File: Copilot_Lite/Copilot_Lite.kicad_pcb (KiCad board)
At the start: 4 copper layers, 65 x 56 mm, 80 parts, among them J1 POWER_MODES, J11 SERIAL_MODE, J12 SERIAL_VOLTAGE_SELECT, J2 JACK_POWER_IN, J3 USB_POWER_IN, J4 USB_PC, J6 5V_ENABLE, J7 SERIAL_AND_GPIO, J8 JACK_POWER_OUT, J9 USB_POWER_OUT, Q1 BSS138, Q2 BUK7M27-80EX, Q3 BUK7M27-80EX, Q4 BSS138, Q5 BSS138, Q6 BSS138, Q7 BSS138, Q8 BSS138, Q9 BSS138, U1 LM74502, U2 LM74502, U3 AP2204K-ADJ, U4 AP2204K-ADJ, U5 FT230XS, U6 SN74LV1T125, U7 SN74LV1T125, U8 SN74LV1T125, U9 SN74LV1T125

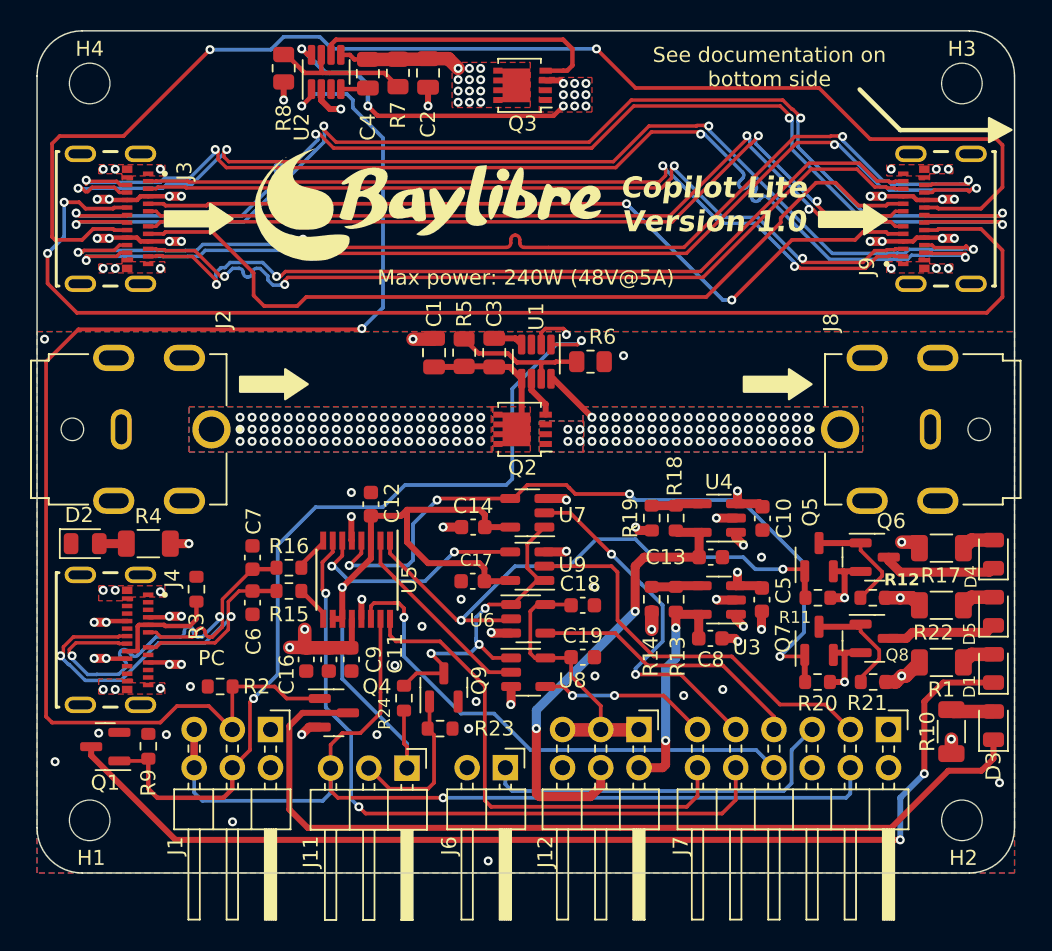
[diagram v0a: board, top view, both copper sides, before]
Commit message: lite: Added a little offset to the USB-C connector shield pins to make sure the connector is well aligned when being soldered.
Signed-off-by: Adrien Ricciardi <aricciardi@baylibre.com>
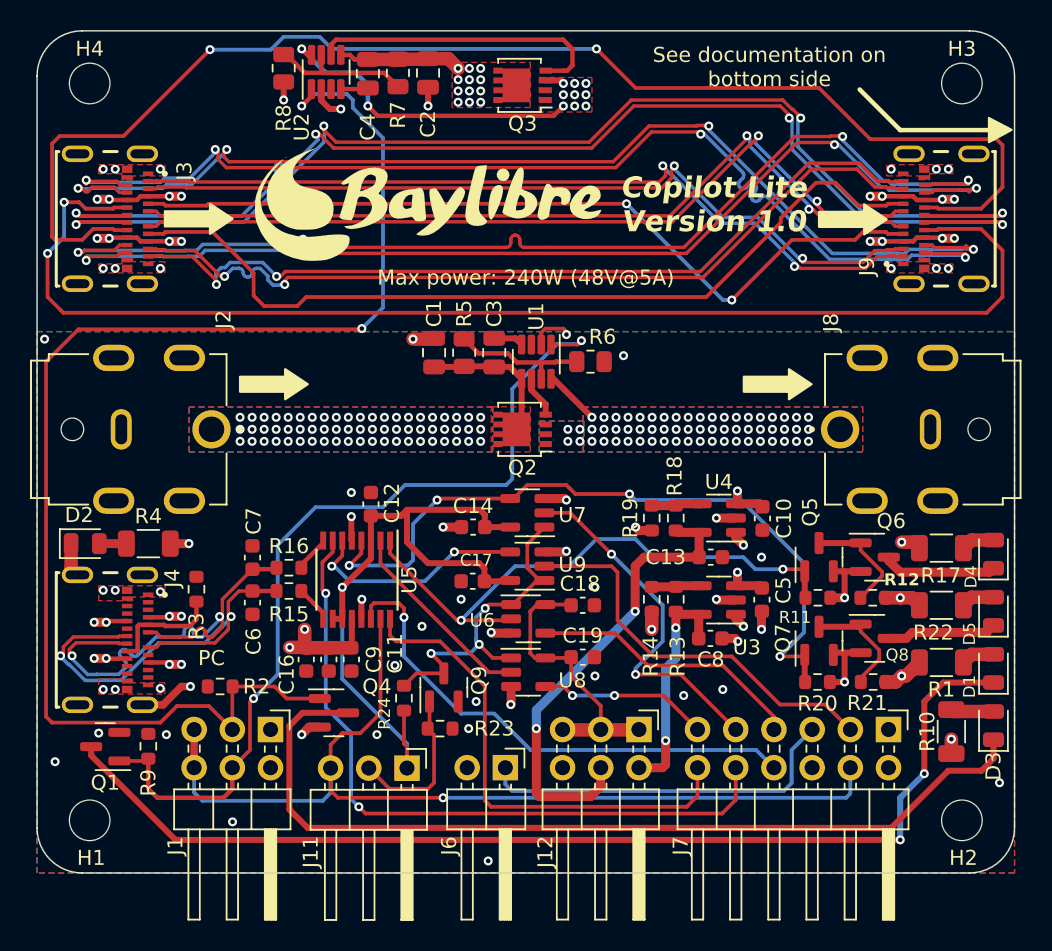
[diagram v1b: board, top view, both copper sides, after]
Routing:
- net GND: track 36.8 -> 42.8 mm
- net /SBU2: track 83.9 -> 84.4 mm
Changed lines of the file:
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@@
     (pad "B12" smd rect (at -2.75 -2.54 90) (size 0.3 0.7) (layers "F.Cu" "F.Paste" "F.Mask")
       (net 2 "GND") (pinfunction "GND_B") (pintype "passive"))
-    (pad "S1" thru_hole oval (at -4.32 0.57 90) (size 1.1 2.1) (drill oval 0.6 1.6) (layers "*.Cu" "*.Mask")
+    (pad "S1" thru_hole oval (at -4.322 0.762 90) (size 1.1 2.1) (drill oval 0.6 1.6) (layers "*.Cu" "*.Mask")
       (net 2 "GND") (pinfunction "SHIELD") (pintype "passive"))
-    (pad "S2" thru_hole oval (at 4.32 0.57 90) (size 1.1 2.1) (drill oval 0.6 1.6) (layers "*.Cu" "*.Mask")
+    (pad "S2" thru_hole oval (at 4.318 0.762 90) (size 1.1 2.1) (drill oval 0.6 1.6) (layers "*.Cu" "*.Mask")
       (net 2 "GND") (pinfunction "SHIELD") (pintype "passive"))
-    (pad "S3" thru_hole oval (at -4.32 -3.43 90) (size 1.1 2.1) (drill oval 0.6 1.6) (layers "*.Cu" "*.Mask")
+    (pad "S3" thru_hole oval (at -4.32 -3.556 90) (size 1.1 2.1) (drill oval 0.6 1.6) (layers "*.Cu" "*.Mask")
       (net 2 "GND") (pinfunction "SHIELD") (pintype "passive"))
-    (pad "S4" thru_hole oval (at 4.32 -3.43 90) (size 1.1 2.1) (drill oval 0.6 1.6) (layers "*.Cu" "*.Mask")
+    (pad "S4" thru_hole oval (at 4.32 -3.556 90) (size 1.1 2.1) (drill oval 0.6 1.6) (layers "*.Cu" "*.Mask")
       (net 2 "GND") (pinfunction "SHIELD") (pintype "passive"))
     (pad "S5" smd rect (at -3.3 -2.54 90) (size 0.5 0.7) (layers "F.Cu" "F.Paste" "F.Mask")
@@
         (effects (font (size 1 1) (thickness 0.15)))
     )
-    (fp_text user "${REFERENCE}" (at 0 0 -90) (layer "F.Fab") hide
+    (fp_text user "${REFERENCE}" (at 0 0 90) (layer "F.Fab") hide
         (effects (font (size 0.8 0.8) (thickness 0.15)))
     )
@@
     (pad "B12" smd rect (at -2.75 -2.54 270) (size 0.3 0.7) (layers "F.Cu" "F.Paste" "F.Mask")
       (net 2 "GND") (pinfunction "GND_B") (pintype "passive"))
-    (pad "S1" thru_hole oval (at -4.32 0.57 270) (size 1.1 2.1) (drill oval 0.6 1.6) (layers "*.Cu" "*.Mask")
+    (pad "S1" thru_hole oval (at -4.322 0.762 270) (size 1.1 2.1) (drill oval 0.6 1.6) (layers "*.Cu" "*.Mask")
       (net 2 "GND") (pinfunction "SHIELD") (pintype "passive"))
-    (pad "S2" thru_hole oval (at 4.32 0.57 270) (size 1.1 2.1) (drill oval 0.6 1.6) (layers "*.Cu" "*.Mask")
+    (pad "S2" thru_hole oval (at 4.318 0.762 270) (size 1.1 2.1) (drill oval 0.6 1.6) (layers "*.Cu" "*.Mask")
       (net 2 "GND") (pinfunction "SHIELD") (pintype "passive"))
-    (pad "S3" thru_hole oval (at -4.32 -3.43 270) (size 1.1 2.1) (drill oval 0.6 1.6) (layers "*.Cu" "*.Mask")
+    (pad "S3" thru_hole oval (at -4.32 -3.556 270) (size 1.1 2.1) (drill oval 0.6 1.6) (layers "*.Cu" "*.Mask")
       (net 2 "GND") (pinfunction "SHIELD") (pintype "passive"))
-    (pad "S4" thru_hole oval (at 4.32 -3.43 270) (size 1.1 2.1) (drill oval 0.6 1.6) (layers "*.Cu" "*.Mask")
+    (pad "S4" thru_hole oval (at 4.32 -3.556 270) (size 1.1 2.1) (drill oval 0.6 1.6) (layers "*.Cu" "*.Mask")
       (net 2 "GND") (pinfunction "SHIELD") (pintype "passive"))
     (pad "S5" smd rect (at -3.3 -2.54 270) (size 0.5 0.7) (layers "F.Cu" "F.Paste" "F.Mask")
@@
         (effects (font (size 1 1) (thickness 0.15)))
     )
-    (fp_text user "${REFERENCE}" (at 0 0 -90) (layer "F.Fab") hide
+    (fp_text user "${REFERENCE}" (at 0 0 90) (layer "F.Fab") hide
         (effects (font (size 0.8 0.8) (thickness 0.15)))
     )
@@
     (pad "B12" smd rect (at -2.75 -2.54 270) (size 0.3 0.7) (layers "F.Cu" "F.Paste" "F.Mask")
       (net 2 "GND") (pinfunction "GND_B") (pintype "passive"))
-    (pad "S1" thru_hole oval (at -4.32 0.57 270) (size 1.1 2.1) (drill oval 0.6 1.6) (layers "*.Cu" "*.Mask")
+    (pad "S1" thru_hole oval (at -4.322 0.762 270) (size 1.1 2.1) (drill oval 0.6 1.6) (layers "*.Cu" "*.Mask")
       (net 2 "GND") (pinfunction "SHIELD") (pintype "passive"))
-    (pad "S2" thru_hole oval (at 4.32 0.57 270) (size 1.1 2.1) (drill oval 0.6 1.6) (layers "*.Cu" "*.Mask")
+    (pad "S2" thru_hole oval (at 4.318 0.762 270) (size 1.1 2.1) (drill oval 0.6 1.6) (layers "*.Cu" "*.Mask")
       (net 2 "GND") (pinfunction "SHIELD") (pintype "passive"))
-    (pad "S3" thru_hole oval (at -4.32 -3.43 270) (size 1.1 2.1) (drill oval 0.6 1.6) (layers "*.Cu" "*.Mask")
+    (pad "S3" thru_hole oval (at -4.32 -3.556 270) (size 1.1 2.1) (drill oval 0.6 1.6) (layers "*.Cu" "*.Mask")
       (net 2 "GND") (pinfunction "SHIELD") (pintype "passive"))
-    (pad "S4" thru_hole oval (at 4.32 -3.43 270) (size 1.1 2.1) (drill oval 0.6 1.6) (layers "*.Cu" "*.Mask")
+    (pad "S4" thru_hole oval (at 4.32 -3.556 270) (size 1.1 2.1) (drill oval 0.6 1.6) (layers "*.Cu" "*.Mask")
       (net 2 "GND") (pinfunction "SHIELD") (pintype "passive"))
     (pad "S5" smd rect (at -3.3 -2.54 270) (size 0.5 0.7) (layers "F.Cu" "F.Paste" "F.Mask")
@@
   (via (at 87.3 83.5) (size 0.6) (drill 0.3) (layers "F.Cu" "B.Cu") (free) (net 1))
   (segment (start 113.175 95.625) (end 113.2 95.6) (width 0.6) (layer "F.Cu") (net 2))
+  (segment (start 67.2625 92.7525) (end 67.688 93.178) (width 0.9) (layer "F.Cu") (net 2))
   (segment (start 100.2 77) (end 100.2 77.2) (width 0.25) (layer "F.Cu") (net 2))
   (segment (start 110.175 89.4) (end 111.475 89.4) (width 0.6) (layer "F.Cu") (net 2))
   (segment (start 98.8 76.8) (end 100 76.8) (width 0.25) (layer "F.Cu") (net 2))
+  (segment (start 74.6 100.6) (end 75.2 100.6) (width 0.5) (layer "F.Cu") (net 2))
   (segment (start 98.7375 91.65) (end 100.15 91.65) (width 0.6) (layer "F.Cu") (net 2))
   (segment (start 83.9 60.875) (end 83.9 61.629962) (width 0.4) (layer "F.Cu") (net 2))
@@
   (segment (start 113.175 96.8) (end 113.175 95.625) (width 0.6) (layer "F.Cu") (net 2))
   (segment (start 96.525 97.05) (end 95.25 97.05) (width 0.6) (layer "F.Cu") (net 2))
+  (segment (start 72.006 101.82) (end 73.38 101.82) (width 0.5) (layer "F.Cu") (net 2))
   (segment (start 119.7625 98.35) (end 118.6 98.35) (width 0.4) (layer "F.Cu") (net 2))
   (segment (start 86.5675 96.1) (end 86.5675 94.8325) (width 0.4) (layer "F.Cu") (net 2))
@@
   (segment (start 118.7 100.3) (end 117.725 100.3) (width 0.4) (layer "F.Cu") (net 2))
   (segment (start 118.6 98.35) (end 118.1 98.35) (width 0.4) (layer "F.Cu") (net 2))
+  (segment (start 67.2625 91.1) (end 67.2625 92.7525) (width 0.9) (layer "F.Cu") (net 2))
+  (segment (start 73.38 101.82) (end 74.6 100.6) (width 0.5) (layer "F.Cu") (net 2))
   (via (at 118.7 100.3) (size 0.6) (drill 0.3) (layers "F.Cu" "B.Cu") (free) (net 2))
   (via (at 118.7 94.7) (size 0.6) (drill 0.3) (layers "F.Cu" "B.Cu") (free) (net 2))
@@
   (arc (start 81.011816 66.484609) (mid 81.099684 66.696741) (end 81.011816 66.908873) (width 0.23) (layer "B.Cu") (net 33))
   (segment (start 70.133884 68.75) (end 70.058883 68.825) (width 0.25) (layer "F.Cu") (net 34))
-  (segment (start 67.65 75.75) (end 65.7 73.8) (width 0.25) (layer "F.Cu") (net 34))
+  (segment (start 124.866116 70.25) (end 124.941116 70.175) (width 0.25) (layer "F.Cu") (net 34))
   (segment (start 67.8 68.4) (end 66.8 68.4) (width 0.25) (layer "F.Cu") (net 34))
   (segment (start 65.7 73.8) (end 65.7 71.8) (width 0.25) (layer "F.Cu") (net 34))
+  (segment (start 68.225 68.825) (end 67.8 68.4) (width 0.25) (layer "F.Cu") (net 34))
+  (segment (start 129.2 74.7) (end 128.15 75.75) (width 0.25) (layer "F.Cu") (net 34))
+  (segment (start 70.058883 68.825) (end 68.225 68.825) (width 0.25) (layer "F.Cu") (net 34))
   (segment (start 127.775 70.175) (end 129.2 71.6) (width 0.25) (layer "F.Cu") (net 34))
-  (segment (start 68.225 68.825) (end 67.8 68.4) (width 0.25) (layer "F.Cu") (net 34))
+  (segment (start 66.75 75.75) (end 66.6 75.6) (width 0.25) (layer "F.Cu") (net 34))
+  (segment (start 65.7 74.7) (end 66.6 75.6) (width 0.25) (layer "F.Cu") (net 34))
   (segment (start 124 70.25) (end 124.866116 70.25) (width 0.25) (layer "F.Cu") (net 34))
   (segment (start 124.941116 70.175) (end 127.775 70.175) (width 0.25) (layer "F.Cu") (net 34))
-  (segment (start 70.058883 68.825) (end 68.225 68.825) (width 0.25) (layer "F.Cu") (net 34))
-  (segment (start 129.2 74.7) (end 128.15 75.75) (width 0.25) (layer "F.Cu") (net 34))
-  (segment (start 128.15 75.75) (end 67.65 75.75) (width 0.25) (layer "F.Cu") (net 34))
-  (segment (start 124.866116 70.25) (end 124.941116 70.175) (width 0.25) (layer "F.Cu") (net 34))
+  (segment (start 70.99 68.75) (end 70.133884 68.75) (width 0.25) (layer "F.Cu") (net 34))
+  (segment (start 128.15 75.75) (end 66.75 75.75) (width 0.25) (layer "F.Cu") (net 34))
+  (segment (start 65.7 73.8) (end 65.7 74.7) (width 0.25) (layer "F.Cu") (net 34))
   (segment (start 129.2 71.6) (end 129.2 74.7) (width 0.25) (layer "F.Cu") (net 34))
-  (segment (start 70.99 68.75) (end 70.133884 68.75) (width 0.25) (layer "F.Cu") (net 34))
   (via (at 65.7 71.8) (size 0.6) (drill 0.3) (layers "F.Cu" "B.Cu") (net 34))
   (via (at 66.8 68.4) (size 0.6) (drill 0.3) (layers "F.Cu" "B.Cu") (net 34))

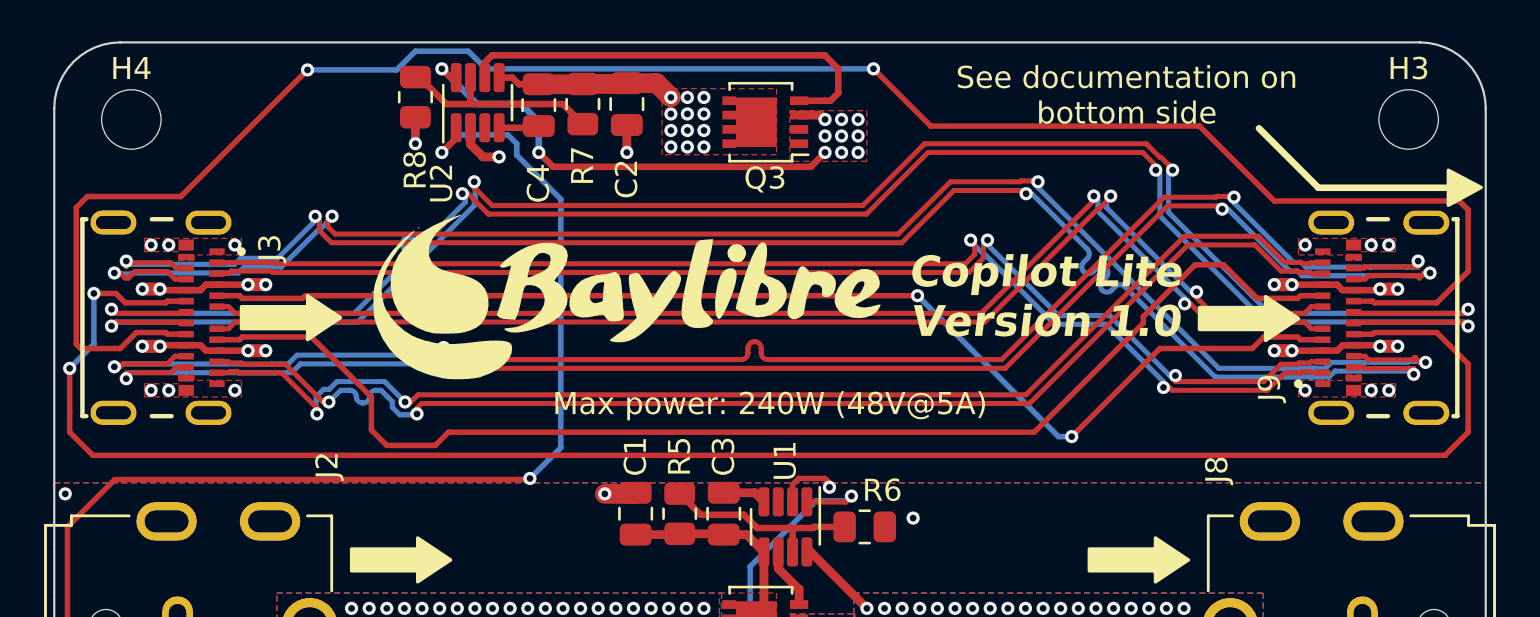
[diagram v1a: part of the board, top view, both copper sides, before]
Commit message: lite: Crossed the USB-C superspeed pairs and SBU signals.
The superspeed pairs and SBU signals of an USB-C cable are crossed.
As Copilot requires two cables, it uncrosses the signals.
That's why Copilot needs to cross again such signals.

Signed-off-by: Adrien Ricciardi <aricciardi@baylibre.com>
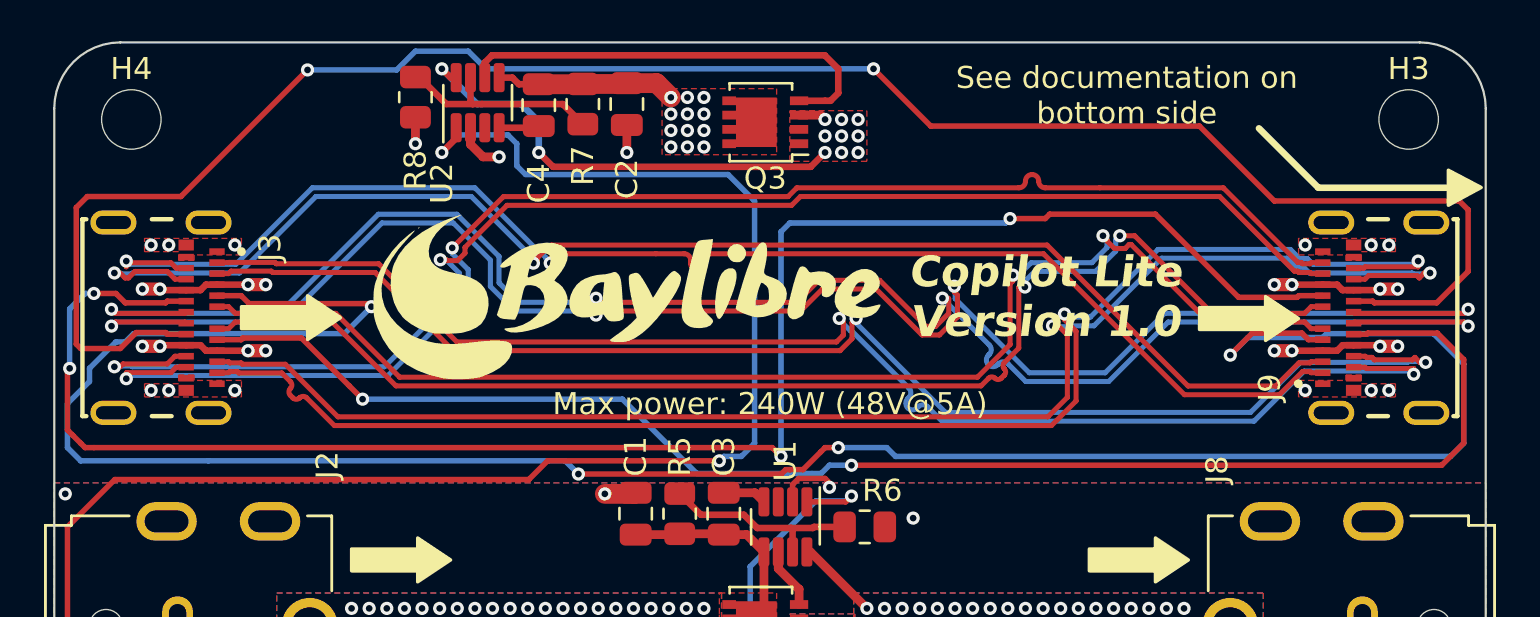
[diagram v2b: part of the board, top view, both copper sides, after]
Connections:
- J9 pad A10: /SSRX2_N -> /SSTX2_N
- J9 pad A11: /SSRX2_P -> /SSTX2_P
- J9 pad A2: /SSTX1_P -> /SSRX1_P
- J9 pad A3: /SSTX1_N -> /SSRX1_N
- J9 pad A8: /SBU1 -> /SBU2
- J9 pad B10: /SSRX1_N -> /SSTX1_N
- J9 pad B11: /SSRX1_P -> /SSTX1_P
- J9 pad B2: /SSTX2_P -> /SSRX2_P
- J9 pad B3: /SSTX2_N -> /SSRX2_N
- J9 pad B8: /SBU2 -> /SBU1
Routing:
- net /CC1: track 54.9 -> 109.9 mm, vias 2 -> 4
- net Net-(J1-Pin_3): track 90.1 -> 107.8 mm
- net /SBU1: track 57.4 -> 69.1 mm, vias 0 -> 2
- net /SSRX2_N: track 56.3 -> 66.1 mm
- net /SSRX2_P: track 56.3 -> 66.1 mm
- net /SSTX1_N: track 54.6 -> 63.8 mm
- net /SSTX1_P: track 54.7 -> 63.8 mm
- net /SSRX1_N: track 73.5 -> 64.8 mm, vias 4 -> 2
- net /SSRX1_P: track 73.4 -> 64.8 mm, vias 4 -> 2
- net /SSTX2_P: track 72.3 -> 65.4 mm, vias 4 -> 2
- net /SSTX2_N: track 72.3 -> 65.4 mm, vias 4 -> 2
- net /SBU2: track 84.4 -> 81.0 mm, vias 2 -> 4
- net /D1_P: track 55.6 -> 58.5 mm
- net /D1_N: track 55.8 -> 58.4 mm
- net /D2_P: track 80.2 -> 81.2 mm
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
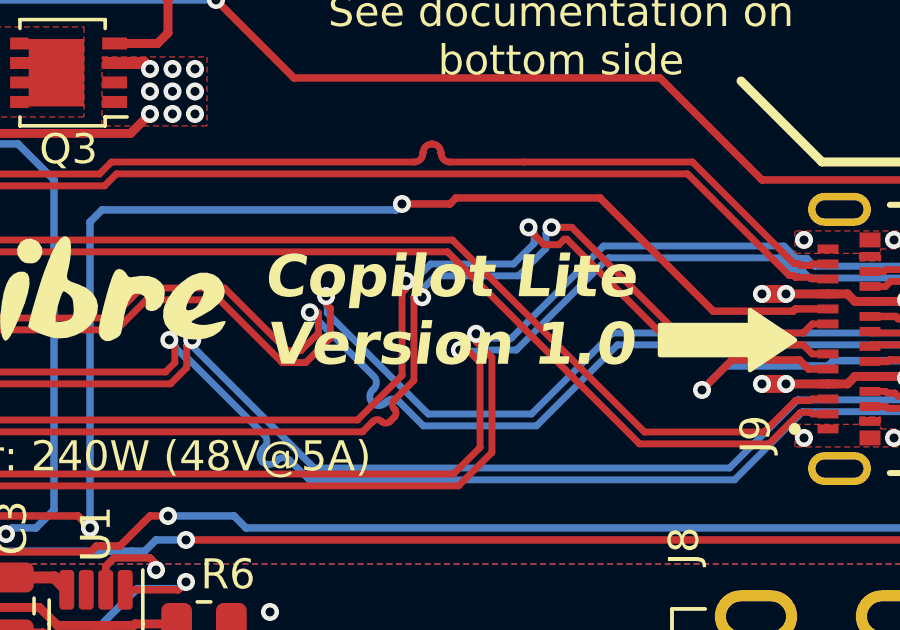
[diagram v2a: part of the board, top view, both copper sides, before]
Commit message: lite: Bumped board version to 1.1.
Signed-off-by: Adrien Ricciardi <aricciardi@baylibre.com>
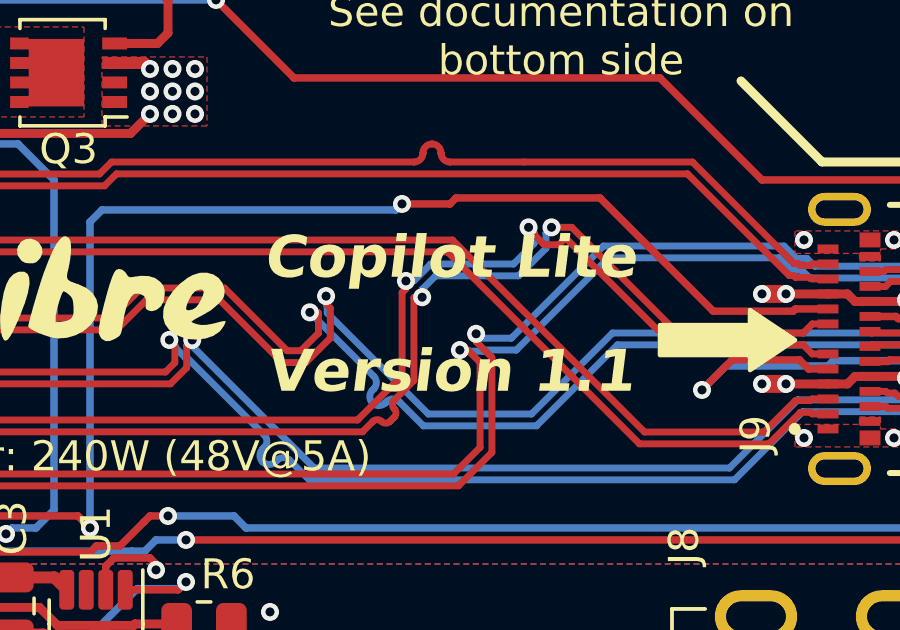
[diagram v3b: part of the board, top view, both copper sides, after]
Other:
- board text added: "Copilot Lite"
- board text added: "Version 1.1"
- board text removed: "Copilot Lite Version 1.0"
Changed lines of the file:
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@@
   (title_block
     (title "Copilot Lite")
-    (date "2023-04-03")
-    (rev "1.0")
+    (date "2023-06-28")
+    (rev "1.1")
     (company "(C) BayLibre")
-    (comment 4 "AISLER Project ID: ENGQIKNM")
   )
   (layers
@@
     (effects (font (size 1 1) (thickness 0.15)) (justify bottom))
   )
-  (gr_text "Copilot Lite\nVersion 1.0" (at 110 70.5) (layer "F.SilkS")
+  (gr_text "Copilot Lite" (at 110 67.6) (layer "F.SilkS")
+    (effects (font (size 1.4 1.4) (thickness 0.3) bold italic) (justify bottom))
+  )
+  (gr_text "Version 1.1" (at 110 71.4) (layer "F.SilkS")
     (effects (font (size 1.4 1.4) (thickness 0.3) bold italic) (justify bottom))
   )
